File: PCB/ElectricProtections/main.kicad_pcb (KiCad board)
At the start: 2 copper layers, 139.8 x 80.3 mm, 87 parts, among them U1 CD4030BE, U2 CD4030BE, U3 CD4030BE, U4 CD4030BE

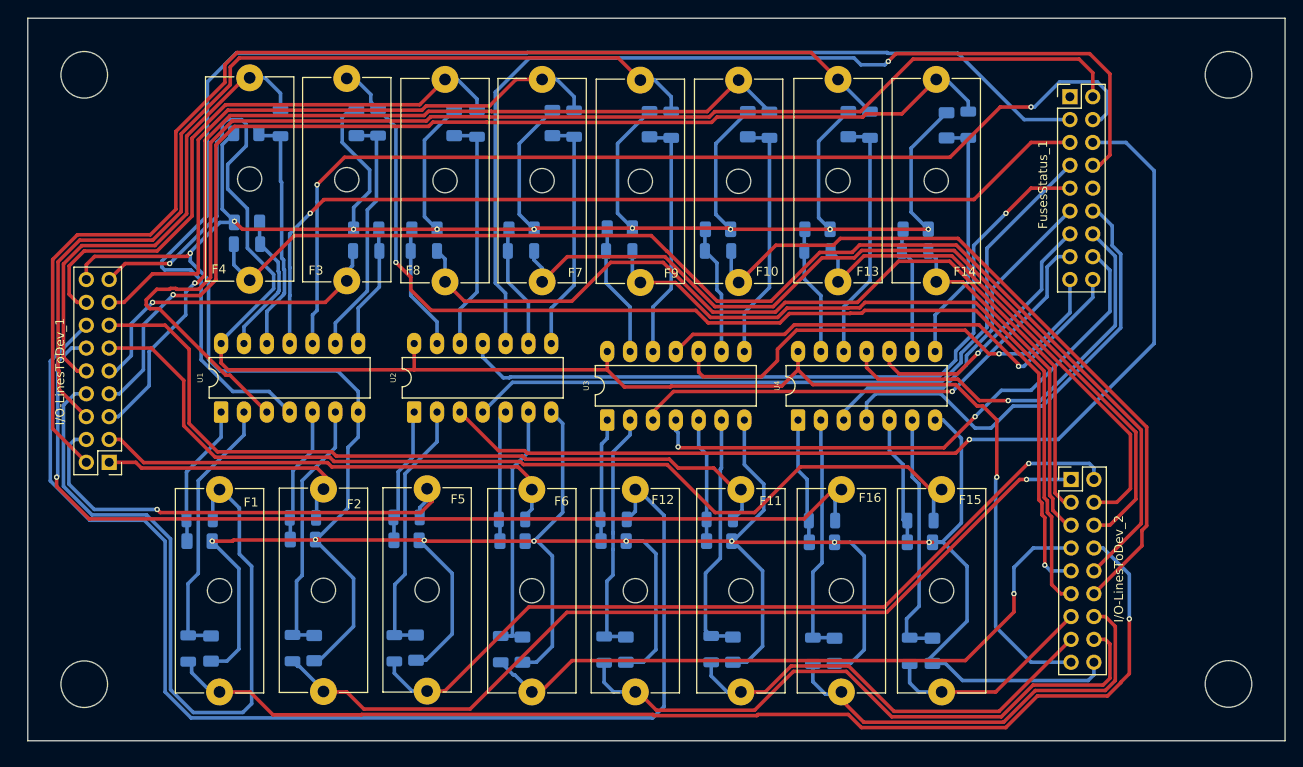
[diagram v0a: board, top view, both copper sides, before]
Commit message: Updates and small enhancements
- PCB size updating
- More space (1.4mm) between the fuses
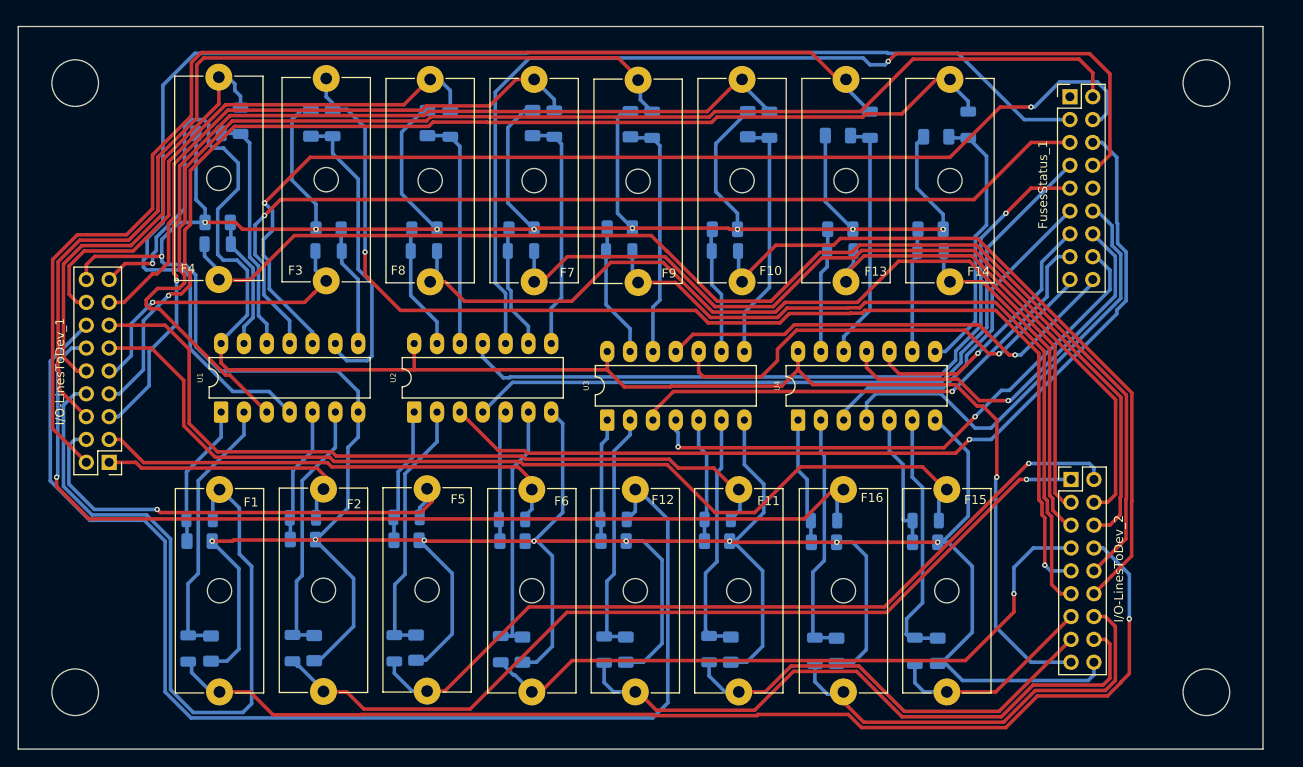
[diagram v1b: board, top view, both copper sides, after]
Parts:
- moved R19 5.05 mm to (109.4, 61.3)
- moved D5 5.05 mm to (107.0, 61.4)
- moved R18 4.45 mm to (99.2, 61.1)
- moved D6 4.19 mm to (95.6, 62.5)
- moved D4 4.18 mm to (109.0, 73.2)
- moved R20 4.18 mm to (109.0, 75.6)
- moved F4 3.43 mm to (96.8, 78.7)
- moved D7 3.26 mm to (96.6, 72.4)
- moved R17 3.26 mm to (96.6, 74.8)
- moved D26 2.97 mm to (120.0, 61.3)
- moved R31 2.97 mm to (122.5, 61.4)
- moved R8 2.54 mm to (165.9, 75.6)
- moved D16 2.54 mm to (165.9, 73.2)
- moved F3 2.29 mm to (108.7, 56.4)
- moved D28 2.20 mm to (131.7, 61.3)
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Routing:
- net P5_CHK: track 111.5 -> 102.9 mm
- net P3_CHK: track 115.2 -> 122.7 mm
- net Net-(D5-K): track 27.5 -> 34.1 mm
- net P4_CHK: track 103.2 -> 109.2 mm
- net P2_CHK: track 149.1 -> 154.1 mm
- net P7: track 72.9 -> 67.9 mm
- net I/O-3 Port: track 126.6 -> 131.3 mm
- net P4: track 53.9 -> 49.6 mm
- net P8: track 66.6 -> 62.6 mm
- net I/O-4 Port: track 137.9 -> 141.1 mm
- net I/O-8 Port: track 100.0 -> 103.0 mm
- net Net-(D13-K): track 27.7 -> 29.8 mm
- net P9_CHK: track 54.8 -> 52.7 mm
- net P3: track 36.3 -> 34.2 mm
- net P13_CHK: track 45.6 -> 43.7 mm
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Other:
- board size 139.8 x 80.3 mm -> 138.4 x 80.3 mm
